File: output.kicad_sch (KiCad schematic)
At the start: 40 parts, among them Q10 Si2306BDS, Q11 IRLB8721PBF, Q12 IRLB8721PBF, Q7 IRLB8721PBF, Q8 IRLB8721PBF, Q9 Si2306BDS, U10 L6398D, U11 ACS758xCB

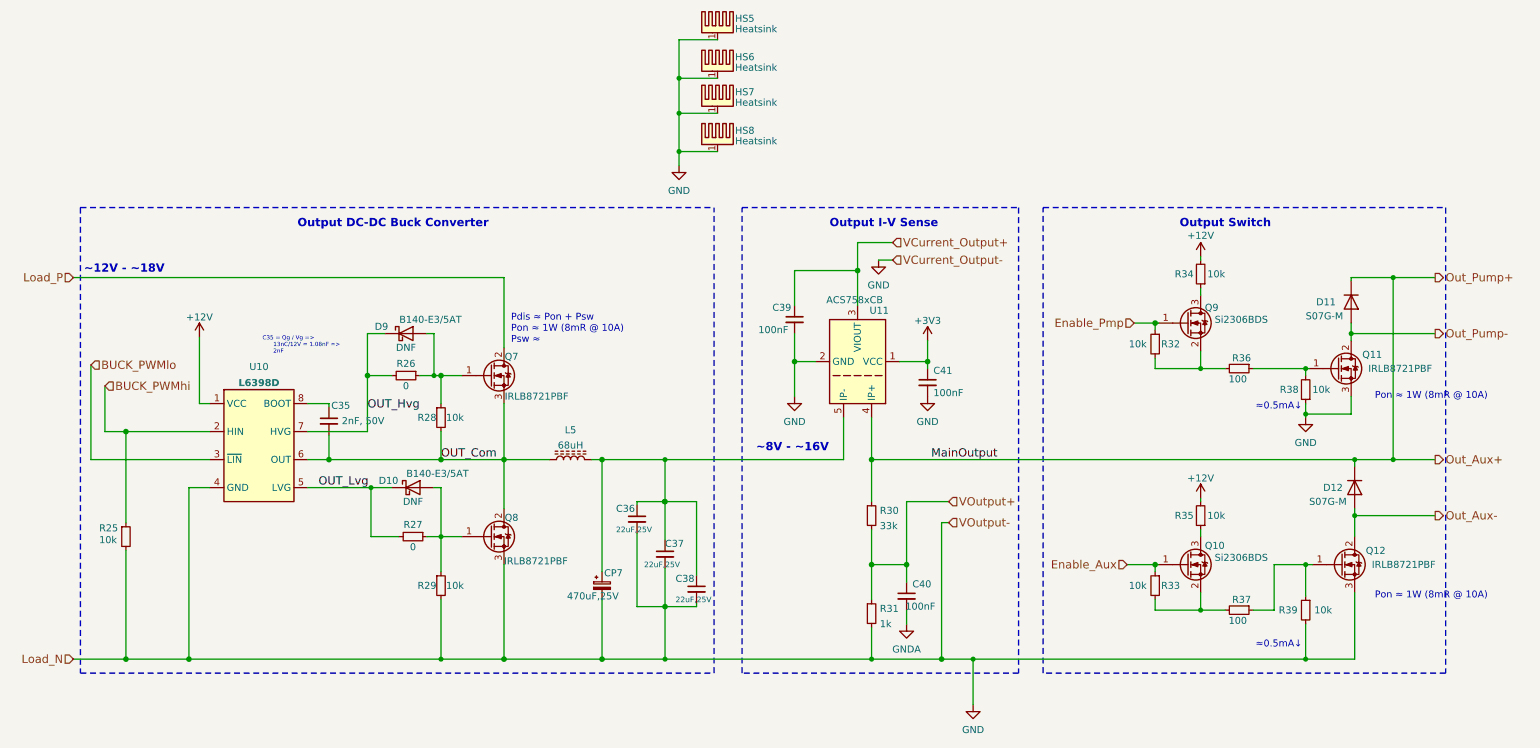
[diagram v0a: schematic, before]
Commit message: Update for Kicad 6-rc; replace 12V reg and cascade; add EEPROM;
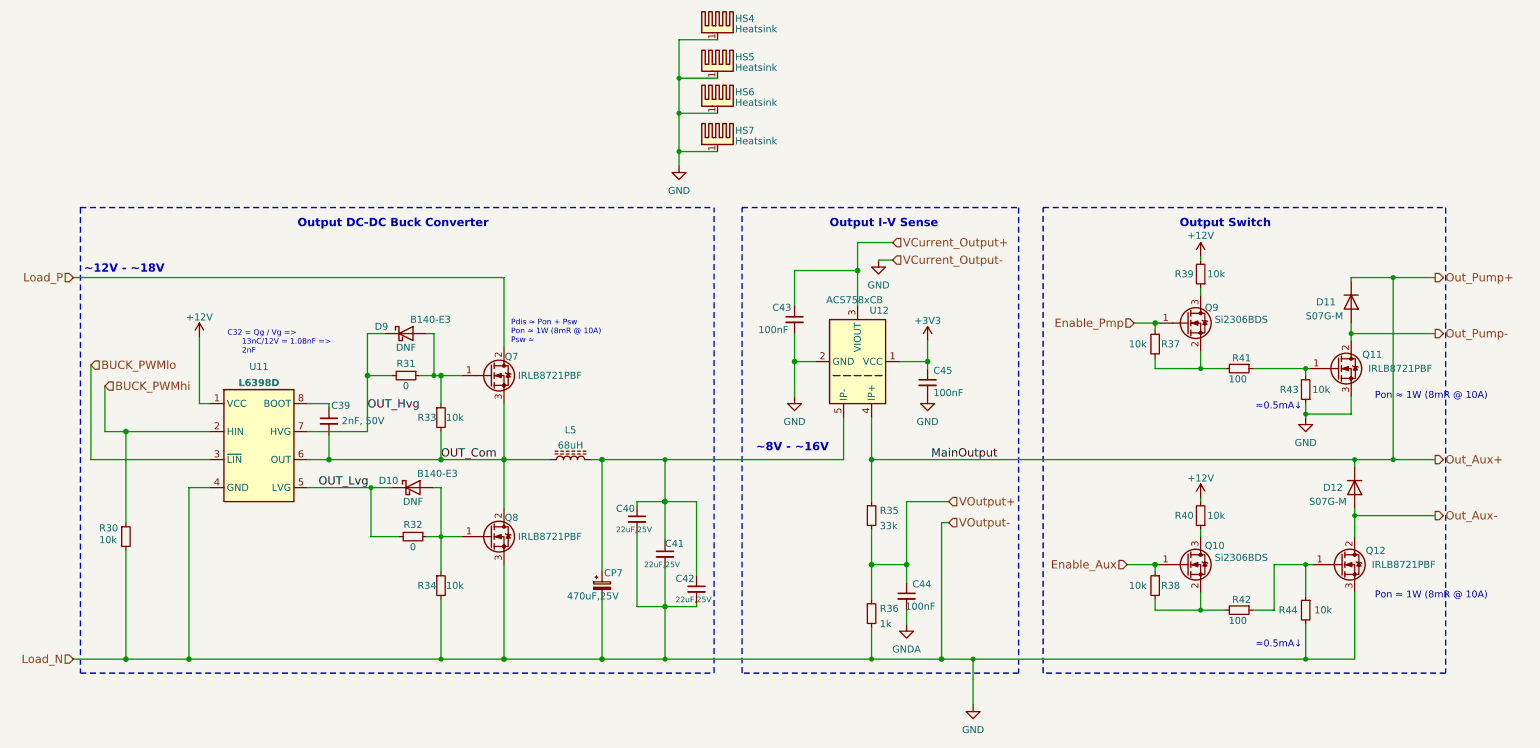
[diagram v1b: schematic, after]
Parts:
- D10, D9: value B140-E3/5AT -> B140-E3
- renumbered C35 to C39, C36 to C40, C37 to C41, C38 to C42, C39 to C43, C40 to C44, C41 to C45, HS5 to HS4, HS6 to HS5, HS7 to HS6, HS8 to HS7, R25 to R30, R26 to R31, R27 to R32, R28 to R33, R29 to R34, R30 to R35, R31 to R36, R32 to R37, R33 to R38, R34 to R39, R35 to R40, R36 to R41, R37 to R42, R38 to R43, R39 to R44, U10 to U11, U11 to U12
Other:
- note added: "C32 = Qg / Vg => 13nC/12V = 1.08nF => 2nF"
- note removed: "C35 = Qg / Vg => 13nC/12V = 1.08nF => 2nF"

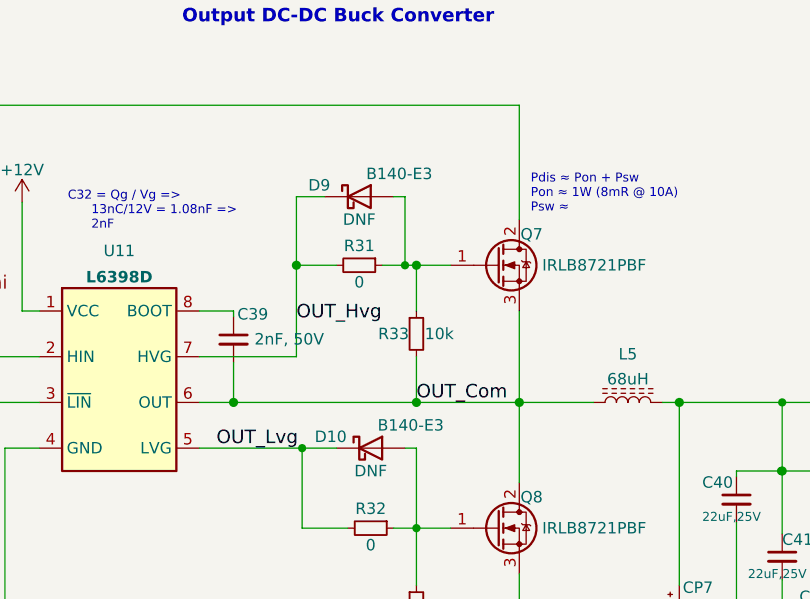
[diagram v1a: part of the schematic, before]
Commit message: Fix diode FP errors, add models; link in regulator error sig; add new coil 3d model; lots of small tweaks
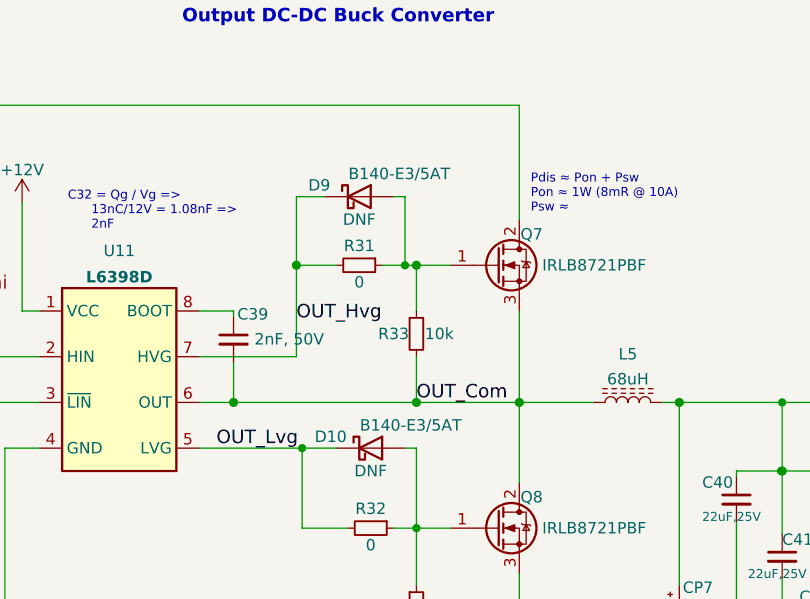
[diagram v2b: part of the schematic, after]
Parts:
- D10, D9: value B140-E3 -> B140-E3/5AT; footprint Diode_SMD:D_SOD-123 -> Diode_SMD:D_SMA
- D11, D12: footprint Diode_SMD:D_SOD-123 -> Diode_SMD:D_SMF
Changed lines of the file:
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@@
     (in_bom no) (on_board yes)
     (property "Reference" "D10" (id 0) (at 80.01 104.14 0))
-    (property "Value" "B140-E3" (id 1) (at 88.9 102.87 0))
-    (property "Footprint" "Diode_SMD:D_SOD-123" (id 2) (at 84.455 105.41 0)
+    (property "Value" "B140-E3/5AT" (id 1) (at 88.9 102.87 0))
+    (property "Footprint" "Diode_SMD:D_SMA" (id 2) (at 84.455 105.41 0)
       (effects (font (size 1.27 1.27)) hide)
     )
@@
     (in_bom no) (on_board yes)
     (property "Reference" "D9" (id 0) (at 78.74 76.2 0))
-    (property "Value" "B140-E3" (id 1) (at 87.63 74.93 0))
-    (property "Footprint" "Diode_SMD:D_SOD-123" (id 2) (at 83.185 77.47 0)
+    (property "Value" "B140-E3/5AT" (id 1) (at 87.63 74.93 0))
+    (property "Footprint" "Diode_SMD:D_SMA" (id 2) (at 83.185 77.47 0)
       (effects (font (size 1.27 1.27)) hide)
     )
@@
       (effects (font (size 1.27 1.27)) (justify left))
     )
-    (property "Footprint" "Diode_SMD:D_SOD-123" (id 2) (at 250.19 71.755 0)
+    (property "Footprint" "Diode_SMD:D_SMF" (id 2) (at 250.19 71.755 0)
       (effects (font (size 1.27 1.27)) hide)
     )
@@
       (effects (font (size 1.27 1.27)) (justify left))
     )
-    (property "Footprint" "Diode_SMD:D_SOD-123" (id 2) (at 250.825 105.41 0)
-      (effects (font (size 1.27 1.27)) hide)
-    )
+    (property "Footprint" "Diode_SMD:D_SMF" (id 2) (at 250.825 105.41 0)
+      (effects (font (size 1.27 1.27)) hide)
+    )

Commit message: Various important tweaks and fixes.
Fix several incorrect capacitor footprints;
Fix slightly incorrect footprint for USB connector;
Add ground vias around MPPT circuit;
Add Zener protection circuit for regulation error input;
Use pin header not socket for Pico Display header;
Fix missing connection to featherwing i2c;
Add in 3d models for USB socket and switch
Update kicad sheet dates;
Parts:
- CP7: footprint Capacitor_THT:C_Radial_D10.0mm_H16.0mm_P5.00mm -> Capacitor_THT:CP_Radial_D8.0mm_P3.50mm
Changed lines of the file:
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@@
   (title_block
     (title "SolarPump v3")
-    (date "2021-11-15")
+    (date "2021-12-03")
     (rev "1.0")
     (company "IvimeyCom")
@@
       (effects (font (size 1.27 1.27)) (justify left))
     )
-    (property "Footprint" "Capacitor_THT:C_Radial_D10.0mm_H16.0mm_P5.00mm" (id 2) (at 118.745 123.19 0)
-      (effects (font (size 1.27 1.27)) hide)
-    )
+    (property "Footprint" "Capacitor_THT:CP_Radial_D8.0mm_P3.50mm" (id 2) (at 118.745 123.19 0)
+      (effects (font (size 1.27 1.27)) hide)
+    )

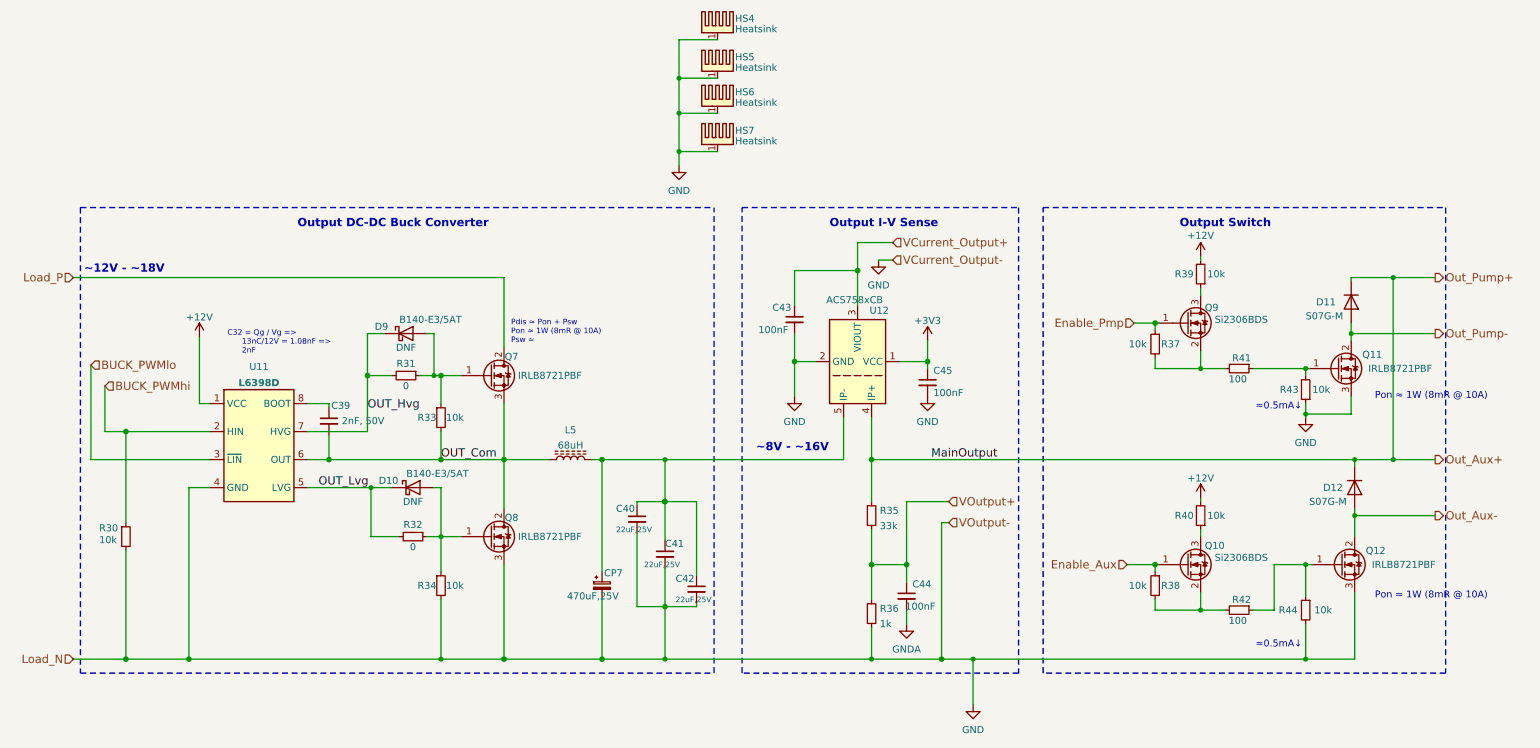
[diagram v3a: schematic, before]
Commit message: Rework with larger display; update component selection; add SWD conn; add RTC chip and QWIIC i2c socket
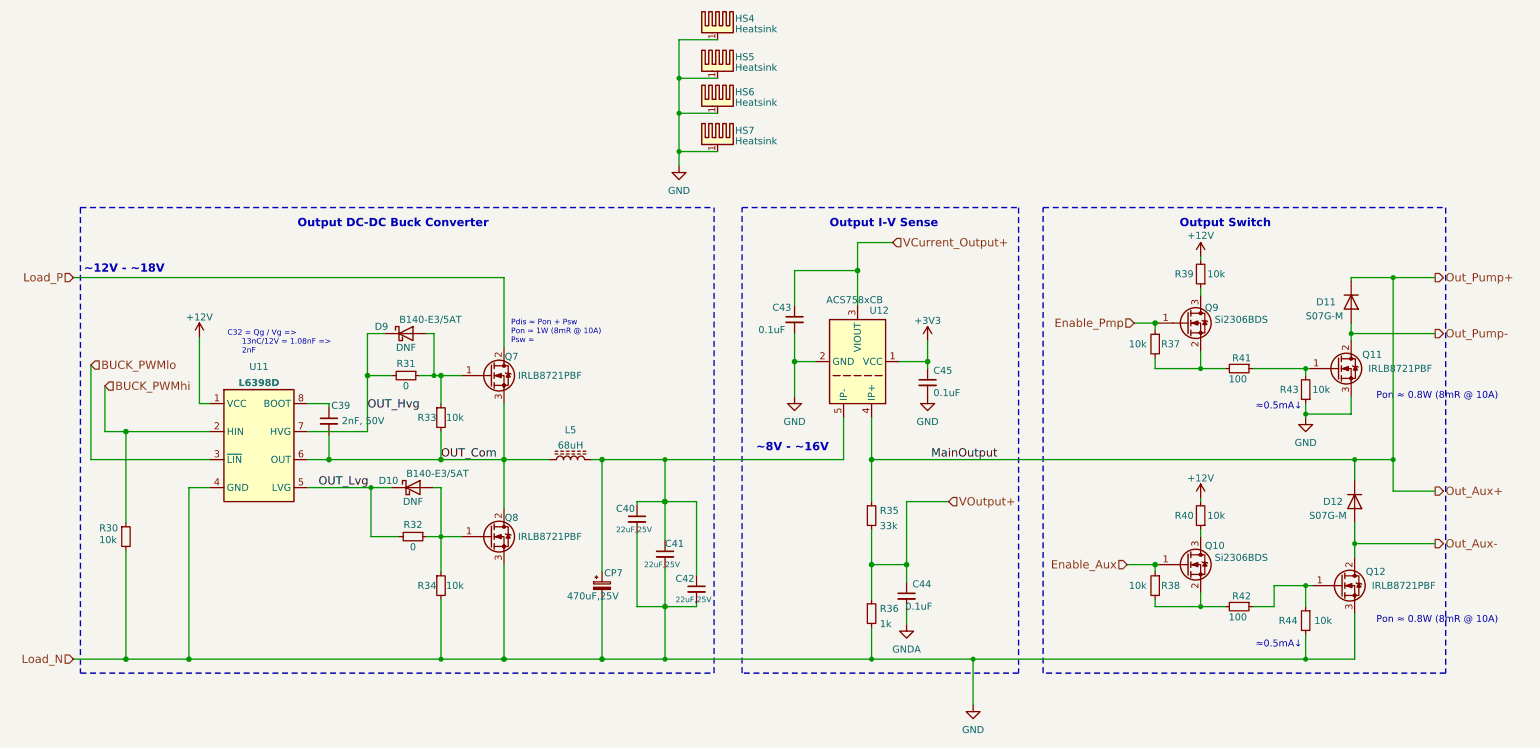
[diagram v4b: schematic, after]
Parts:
- C39: Supl Price 0.07 -> 0.077
- C40, C41, C42: Mfr Samsung -> Samsung Electro-Mechanics; Mfr Part No CL32A226KAJNNNE -> CL21A226MAQNNNE; Supl Part No 187-CL32A226KAJNNNE -> 187-CL21A226MAQNNNE; Supl Price 0.411 -> 0.25
- C43, C44, C45: value 100nF -> 0.1uF; Mfr KEMET -> Samsung Electro-Mechanics; Mfr Part No C0402C104K8R7411 -> CL21B104KACNNND; Supl Part No 80-C0402C104K8R7411 -> 187-CL21B104KACNNND
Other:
- note added: "Pon ≈ 0.8W (8mR @ 10A)"
- note removed: "Pon ≈ 1W (8mR @ 10A)"
- moved on the sheet: D12, Q12, R42, R44

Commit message: More updates to regularise property names
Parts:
- C39: Manuf (none) -> Samsung Electro-Mechanics; Mfr Samsung Electro-Mechanics -> (none); Mfr Part No CL21B202KBANNNC -> (none); Part (none) -> CL21B202KBANNNC; Supl Mouser -> (none); Supl Part No 187-CL21B202KBANNNC -> (none); Supl Price 0.077 -> (none); Suppl Mouser -> (none); Vendor (none) -> Mouser; Vendor Cost (none) -> 0.077; Vendor SKU (none) -> 187-CL21B202KBANNNC
- C40, C41, C42: Manuf (none) -> Samsung Electro-Mechanics; Mfr Samsung Electro-Mechanics -> (none); Mfr Part No CL21A226MAQNNNE -> (none); Part (none) -> CL21A226MAQNNNE; Supl Mouser -> (none); Supl Part No 187-CL21A226MAQNNNE -> (none); Supl Price 0.25 -> (none); Vendor (none) -> Mouser; Vendor Cost (none) -> 0.25; Vendor SKU (none) -> 187-CL21A226MAQNNNE
- C43, C44, C45: Manuf (none) -> Samsung Electro-Mechanics; Mfr Samsung Electro-Mechanics -> (none); Mfr Part No CL21B104KACNNND -> (none); Part (none) -> CL21B104KACNNND; Supl Mouser -> (none); Supl Part No 187-CL21B104KACNNND -> (none); Supl Price 0.016 -> (none); Vendor (none) -> Mouser; Vendor Cost (none) -> 0.016; Vendor SKU (none) -> 187-CL21B104KACNNND
- CP7: Manuf (none) -> KEMET; Mfr KEMET -> (none); Mfr Part No ESW477M025AH2AA -> (none); Part (none) -> ESW477M025AH2AA; Supl Mouser -> (none); Supl Part No 80-ESW477M025AH2AA -> (none); Supl Price 0.382 -> (none); Vendor (none) -> Mouser; Vendor Cost (none) -> 0.382; Vendor SKU (none) -> 80-ESW477M025AH2AA
- D10, D9: value B140-E3/5AT -> B140-E3; Manuf (none) -> Vishay; Mfr Vishay -> (none); Mfr Part No B140-E3 -> (none); Part (none) -> B140-E3/5AT; Supl Mouser -> (none); Supl Part No 625-B140-E3 -> (none); Supl Price 0.277 -> (none); Vendor (none) -> Mouser; Vendor Cost (none) -> 0.277; Vendor SKU (none) -> 625-B140-E3
- D11, D12: Manuf (none) -> Vishay; Mfr Vishay -> (none); Mfr Part No S07G-M -> (none); Part (none) -> S07G-M; Supl Mouser -> (none); Supl Part No 78-S07G-M-18 -> (none); Supl Price 0.29 -> (none); Vendor (none) -> Mouser; Vendor Cost (none) -> 0.29; Vendor SKU (none) -> 78-S07G-M-18
- Q10, Q9: Manuf (none) -> Vishay; Mfr Vishay -> (none); Mfr Part No SI2306BDS-T1-E3 -> (none); Part (none) -> SI2306BDS-T1-E3; Supl Mouser -> (none); Supl Part No 781-SI2306BDS-E3 -> (none); Supl Price 0.496 -> (none); Vendor (none) -> Mouser; Vendor Cost (none) -> 0.496; Vendor SKU (none) -> 781-SI2306BDS-E3
- Q11, Q12, Q7, Q8: Manuf (none) -> Infineon / IR; Mfr Infineon / IR -> (none); Mfr Part No IRLB8721PBF -> (none); Part (none) -> IRLB8721PBF; Supl Mouser -> (none); Supl Part No 942-IRLB8721PBF -> (none); Supl Price 0.824 -> (none); Vendor (none) -> Mouser; Vendor Cost (none) -> 0.824; Vendor SKU (none) -> 942-IRLB8721PBF
- R30, R33, R34, R37, R38, R39, R40, R41, R42, R43, R44: Manuf (none) -> Yageo; Mfr Yageo -> (none); Mfr Part No AC0805FR-0710KL -> (none); Part (none) -> AC0805FR-0710KL; Supl Mouser -> (none); Supl Part No 603-AC0805FR-0710KL -> (none); Supl Price 0.077 -> (none); Vendor (none) -> Mouser; Vendor Cost (none) -> 0.077; Vendor SKU (none) -> 603-AC0805FR-0710KL
- R31, R32: Manuf (none) -> Yageo; Mfr Yageo -> (none); Mfr Part No RC0805FR-070RL -> (none); Part (none) -> RC0805FR-070RL; Supl Mouser -> (none); Supl Part No 603-RC0805FR-070RL -> (none); Supl Price 0.077 -> (none); Vendor (none) -> Mouser; Vendor Cost (none) -> 0.077; Vendor SKU (none) -> 603-RC0805FR-070RL
- R35: Manuf (none) -> Yageo; Mfr Yageo -> (none); Mfr Part No RC0805FR-0733KL -> (none); Part (none) -> RC0805FR-0733KL; Supl Mouser -> (none); Supl Part No 603-RC0805FR-0733KL -> (none); Supl Price 0.077 -> (none); Vendor (none) -> Mouser; Vendor Cost (none) -> 0.077; Vendor SKU (none) -> 603-RC0805FR-0733KL
- R36: Manuf (none) -> Yageo; Mfr Yageo -> (none); Mfr Part No RC0805FR-071KL -> (none); Part (none) -> RC0805FR-071KL; Supl Mouser -> (none); Supl Part No 603-RC0805FR-071KL -> (none); Supl Price 0.077 -> (none); Vendor (none) -> Mouser; Vendor Cost (none) -> 0.077; Vendor SKU (none) -> 603-RC0805FR-071KL
- U11: Manuf (none) -> STMicroelectronics; Mfr STMicroelectronics -> (none); Mfr Part No L6398D -> (none); Part (none) -> L6398D; Supl Mouser -> (none); Supl Part No 511-L6398D -> (none); Supl Price 1.32 -> (none); Vendor (none) -> Mouser; Vendor Cost (none) -> 1.32; Vendor SKU (none) -> 511-L6398D

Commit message: Fix some errors in the design (esp net-tie in wrong place)
 - correct led, diode footprints & model
 - fix fuse holder (bad hole spec)
 - update oled mod
 - update EC11 mod
 - add Blender models of case (xz compressed)
 - more updated gerbers (not current!)
 - improve layout of front panel pcb
 - delete unused files
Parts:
- C40, C41, C42: footprint Capacitor_SMD:C_1210_3225Metric_Pad1.33x2.70mm_HandSolder -> Capacitor_SMD:C_0805_2012Metric_Pad1.18x1.45mm_HandSolder
- HS4, HS5, HS6, HS7: footprint MountingHole:MountingHole_2.2mm_M2_Pad_Via -> MountingHole:MountingHole_2.7mm_M2.5_Pad_Via
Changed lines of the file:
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@@
   (title_block
     (title "SolarPump v3")
-    (date "2021-12-10")
-    (rev "1.0")
+    (date "2022-03-09")
+    (rev "1.1")
     (company "IvimeyCom")
   )
@@
       (effects (font (size 1 1)) (justify left))
     )
-    (property "Footprint" "Capacitor_SMD:C_1210_3225Metric_Pad1.33x2.70mm_HandSolder" (id 2) (at 130.175 117.475 0)
+    (property "Footprint" "Capacitor_SMD:C_0805_2012Metric_Pad1.18x1.45mm_HandSolder" (id 2) (at 130.175 117.475 0)
       (effects (font (size 1.27 1.27)) hide)
     )
@@
       (effects (font (size 1.27 1.27)) (justify left))
     )
-    (property "Footprint" "MountingHole:MountingHole_2.2mm_M2_Pad_Via" (id 2) (at 140.0048 22.8984 0)
+    (property "Footprint" "MountingHole:MountingHole_2.7mm_M2.5_Pad_Via" (id 2) (at 140.0048 22.8984 0)
       (effects (font (size 1.27 1.27)) hide)
     )
@@
       (effects (font (size 1 1)) (justify left))
     )
-    (property "Footprint" "Capacitor_SMD:C_1210_3225Metric_Pad1.33x2.70mm_HandSolder" (id 2) (at 125.095 111.125 0)
+    (property "Footprint" "Capacitor_SMD:C_0805_2012Metric_Pad1.18x1.45mm_HandSolder" (id 2) (at 125.095 111.125 0)
       (effects (font (size 1.27 1.27)) hide)
     )
@@
       (effects (font (size 1.27 1.27)) (justify left))
     )
-    (property "Footprint" "MountingHole:MountingHole_2.2mm_M2_Pad_Via" (id 2) (at 140.0048 29.8834 0)
+    (property "Footprint" "MountingHole:MountingHole_2.7mm_M2.5_Pad_Via" (id 2) (at 140.0048 29.8834 0)
       (effects (font (size 1.27 1.27)) hide)
     )
@@
       (effects (font (size 1 1)) (justify left))
     )
-    (property "Footprint" "Capacitor_SMD:C_1210_3225Metric_Pad1.33x2.70mm_HandSolder" (id 2) (at 135.89 123.825 0)
+    (property "Footprint" "Capacitor_SMD:C_0805_2012Metric_Pad1.18x1.45mm_HandSolder" (id 2) (at 135.89 123.825 0)
       (effects (font (size 1.27 1.27)) hide)
     )
@@
       (effects (font (size 1.27 1.27)) (justify left))
     )
-    (property "Footprint" "MountingHole:MountingHole_2.2mm_M2_Pad_Via" (id 2) (at 140.0048 43.18 0)
+    (property "Footprint" "MountingHole:MountingHole_2.7mm_M2.5_Pad_Via" (id 2) (at 140.0048 43.18 0)
       (effects (font (size 1.27 1.27)) hide)
     )
@@
       (effects (font (size 1.27 1.27)) (justify left))
     )
-    (property "Footprint" "MountingHole:MountingHole_2.2mm_M2_Pad_Via" (id 2) (at 140.0048 36.2334 0)
-      (effects (font (size 1.27 1.27)) hide)
-    )
+    (property "Footprint" "MountingHole:MountingHole_2.7mm_M2.5_Pad_Via" (id 2) (at 140.0048 36.2334 0)
+      (effects (font (size 1.27 1.27)) hide)
+    )

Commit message: Schematic + pcb 1.3.3
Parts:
- HS4, HS5, HS6, HS7: value Heatsink -> HSink
- R31, R32: value 0 -> 0R
- R35: value 33k -> 33K,1%
- R41, R42: value 100 -> 100R; Part AC0805FR-0710KL -> RC0805FR-07100RL; Vendor Cost 0.077 -> 0.08; Vendor SKU 603-AC0805FR-0710KL -> 603-RC0805FR-07100RL
